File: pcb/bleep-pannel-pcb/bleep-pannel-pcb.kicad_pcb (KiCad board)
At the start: 2 copper layers, 80 x 36.3 mm, 23 parts, among them J1 CON_LED

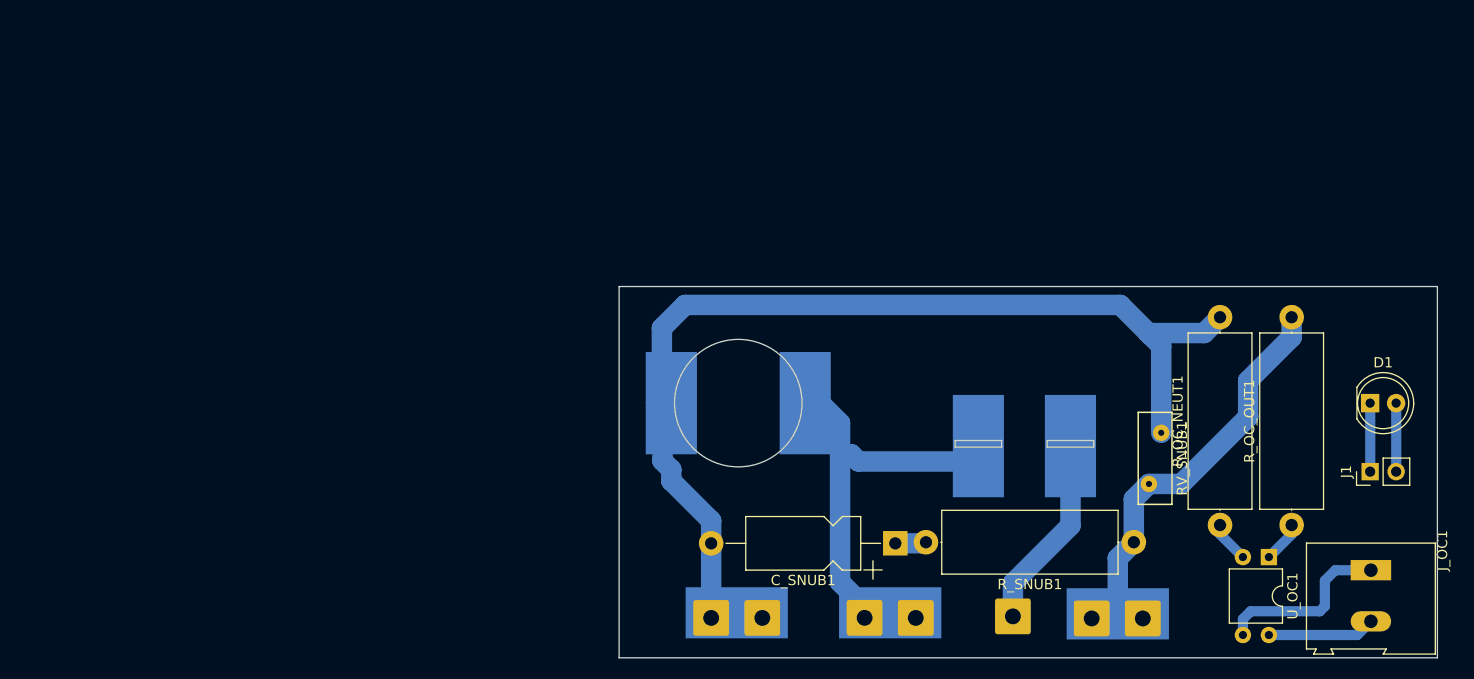
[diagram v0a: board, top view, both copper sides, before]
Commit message: Updating for origin issues
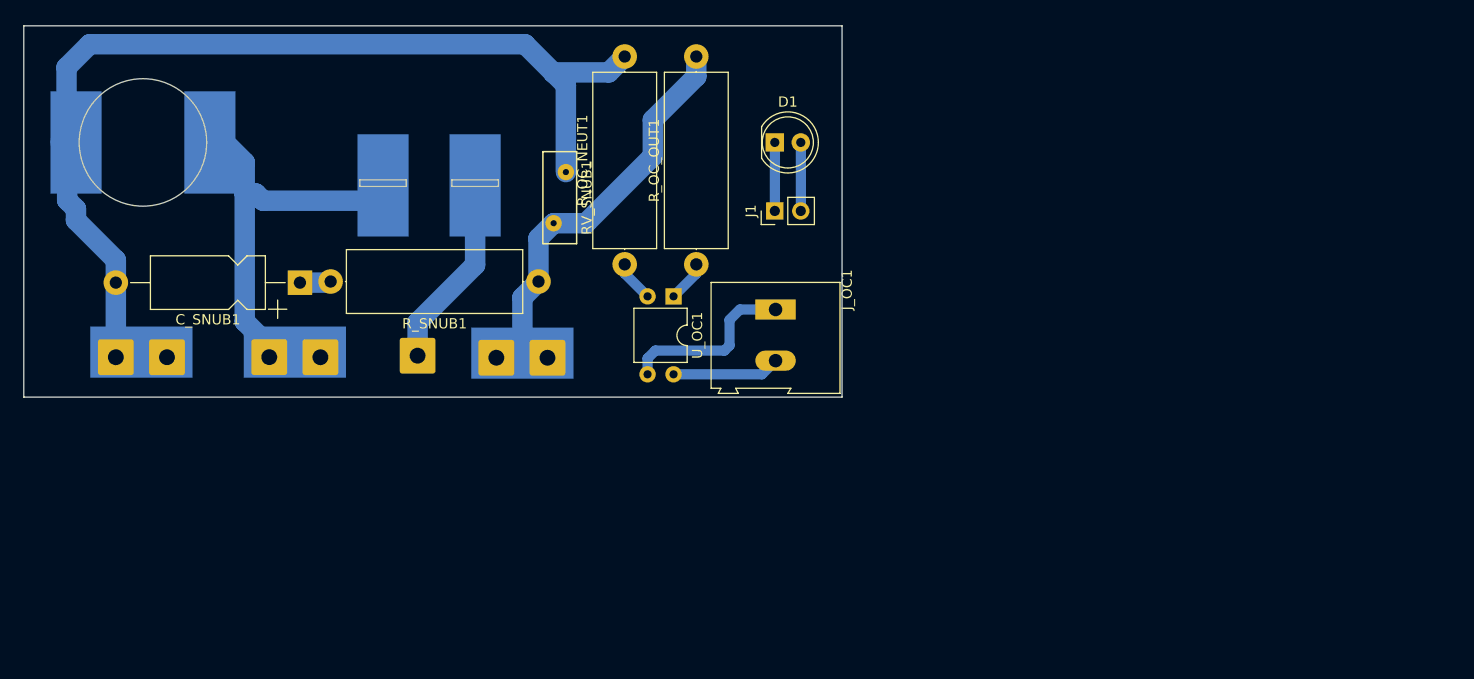
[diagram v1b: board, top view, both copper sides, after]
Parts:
- moved D1 63.5 mm to (73.7, 11.9)
- moved J1 63.5 mm to (73.7, 18.6)
- moved U_OC1 63.5 mm to (63.8, 27.0)
- moved CON_NEU_IN1 63.5 mm to (9.30, 32.9)
- moved CON_NEU_OUT1 63.5 mm to (14.3, 32.9)
- moved CON_OUT_IN1 63.5 mm to (46.5, 33.0)
- moved CON_OUT_OUT1 63.5 mm to (51.5, 33.0)
- moved CON_SW1 63.5 mm to (38.8, 32.8)
- moved CON_VAC_IN1 63.5 mm to (29.3, 32.9)
- moved CON_VAC_OUT1 63.5 mm to (24.3, 32.9)
- moved C_SNUB1 63.5 mm to (27.3, 25.6)
- moved J_OC1 63.5 mm to (73.8, 28.2)
- moved PAD_NEU1 63.5 mm to (11.8, 32.4)
- moved PAD_OUT1 63.5 mm to (49.0, 32.5)
- moved PAD_SWL2 63.5 mm to (5.40, 11.9)
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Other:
- outline, holes or cut-outs redrawn

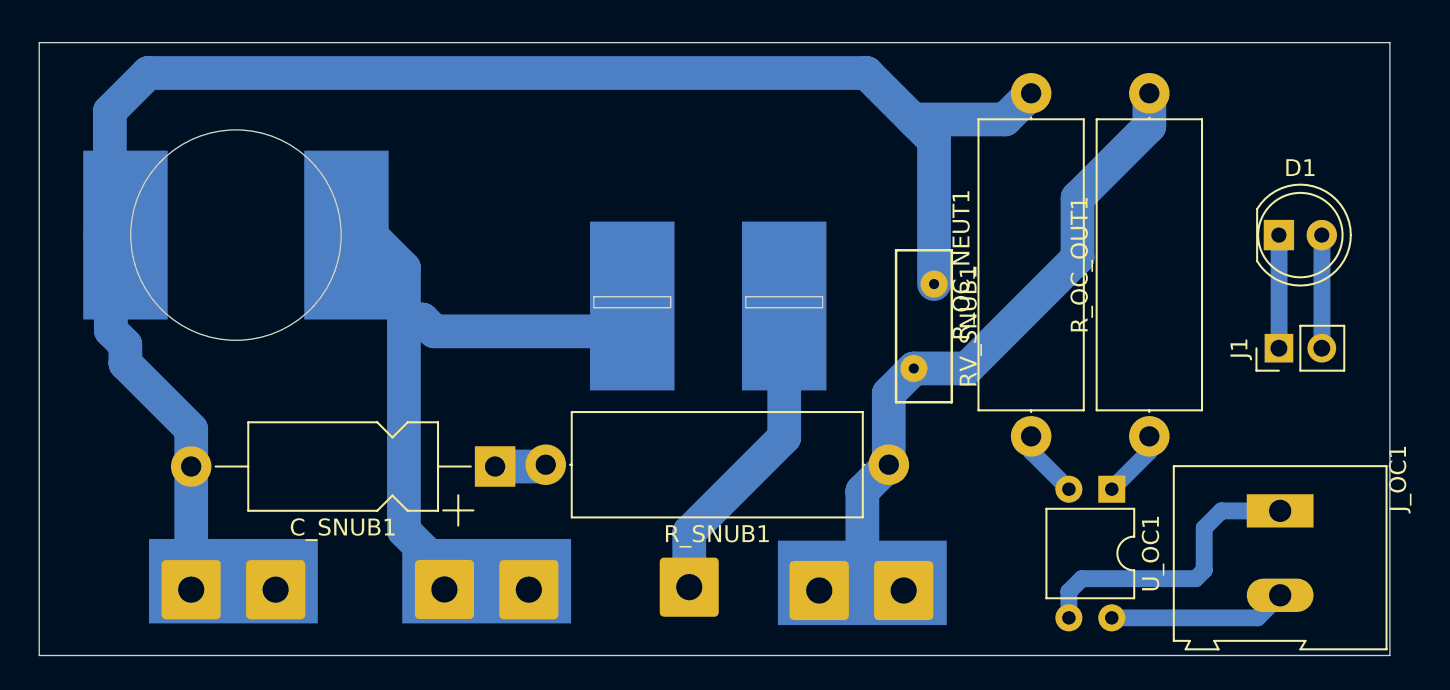
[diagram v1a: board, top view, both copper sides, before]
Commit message: Minor updates to component sizes
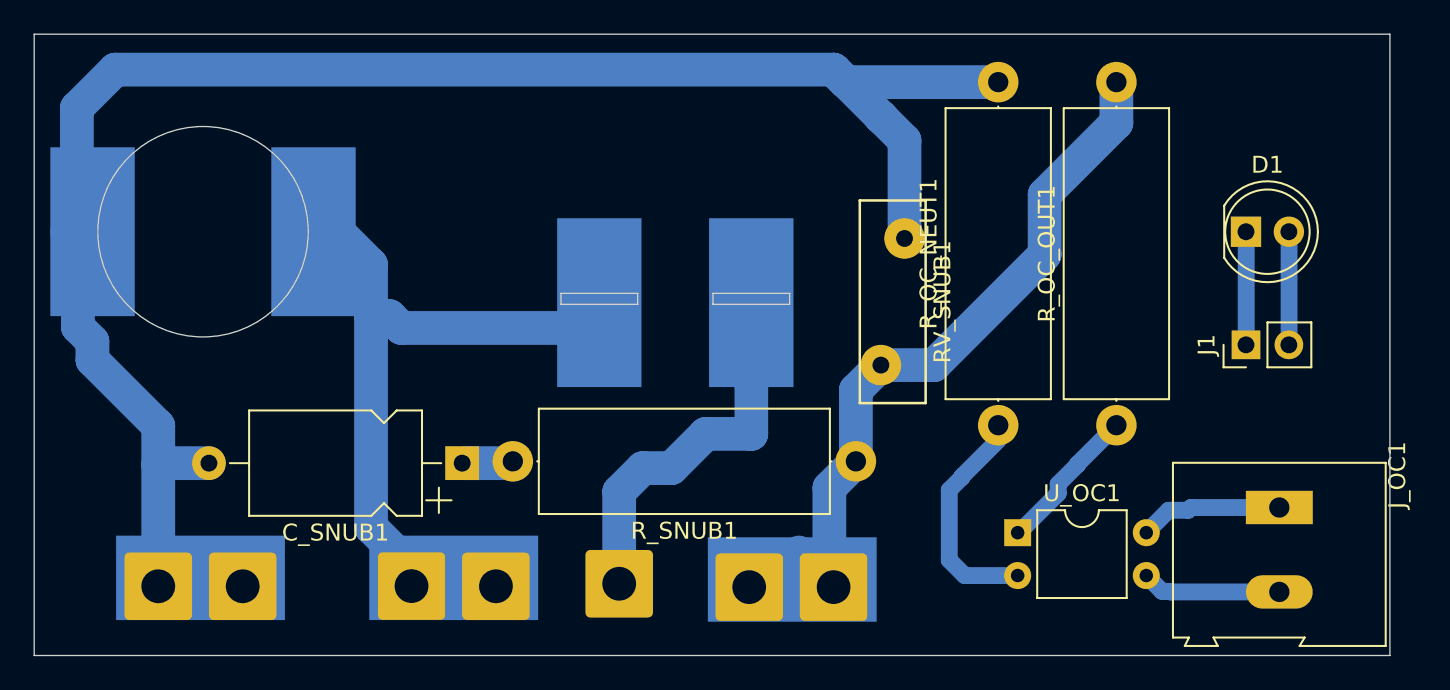
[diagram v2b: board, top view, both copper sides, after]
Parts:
- C_SNUB1: footprint Capacitor_THT:CP_Axial_L11.0mm_D5.0mm_P18.00mm_Horizontal -> Capacitor_THT:CP_Axial_L10.0mm_D6.0mm_P15.00mm_Horizontal
- RV_SNUB1: footprint Varistor:RV_Disc_D9mm_W3.3mm_P5mm -> Varistor:RV_Disc_D12mm_W3.9mm_P7.5mm
- moved U_OC1 6.14 mm to (58.2, 29.5), turned to 0 degrees
- moved CON_OUT_IN1 4.15 mm to (42.3, 32.8)
- moved CON_OUT_OUT1 4.15 mm to (47.3, 32.8)
- moved CON_SW1 4.15 mm to (34.6, 32.6)
- moved PAD_OUT1 4.15 mm to (44.9, 32.3)
- moved R_OC_OUT1 2.06 mm to (64.1, 23.2)
- moved R_OC_NEUT1 2.06 mm to (57.1, 23.2)
- moved R_SNUB1 1.96 mm to (48.7, 25.3)
- moved D1 1.96 mm to (71.8, 11.7)
- moved J1 1.96 mm to (71.8, 18.4)
- moved PAD_SWL1 1.96 mm to (16.5, 11.7)
- moved RV_SNUB1 1.96 mm to (50.1, 19.6)
- moved CON_NEU_IN1 1.96 mm to (7.35, 32.7)
- moved CON_NEU_OUT1 1.96 mm to (12.3, 32.7)
- moved PAD_NEU1 1.96 mm to (9.85, 32.2)
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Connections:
- U_OC1 pad 3: Net-(J_OC1-Pin_1) -> Net-(J_OC1-Pin_2)
- U_OC1 pad 4: Net-(J_OC1-Pin_2) -> Net-(J_OC1-Pin_1)
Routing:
- net Net-(J_OC1-Pin_1): track 17.5 -> 8.50 mm
- net Net-(R_OC_NEUT1-Pad1): track 4.06 -> 12.7 mm
- net Net-(R_OC_OUT1-Pad1): track 4.05 -> 8.83 mm
- net Net-(CON_SW1-Pin_1): track 17.5 -> 21.0 mm
- net NEUT: track 97.0 -> 99.9 mm
- net Net-(J_OC1-Pin_2): track 10.5 -> 8.28 mm
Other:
- board size 80 x 36.3 mm -> 80.3 x 36.8 mm
